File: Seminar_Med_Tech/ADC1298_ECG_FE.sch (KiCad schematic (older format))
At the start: 54 parts, among them J6 DB15_F-RA

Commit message: update anno
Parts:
- J4: renamed from J?; footprint (none) -> Pin_Headers:Pin_Header_Straight_1x02_Pitch2.54mm
- J8: renamed from J?; footprint (none) -> Pin_Headers:Pin_Header_Straight_1x10_Pitch2.54mm
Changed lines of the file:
@@
 AGND
 $Comp
-L CONN_01X10 J?
+L CONN_01X10 J8
 U 1 1 5947AEC5
 P 800 2100
-F 0 "J?" H 800 2650 50  0000 C CNN
+F 0 "J8" H 800 2650 50  0000 C CNN
 F 1 "CONN_01X10" V 900 2100 50  0000 C CNN
-F 2 "" H 800 2100 50  0001 C CNN
+F 2 "Pin_Headers:Pin_Header_Straight_1x10_Pitch2.54mm" H 800 2100 50  0001 C CNN
 F 3 "" H 800 2100 50  0001 C CNN
 	1    800  2100
@@
 Connection ~ 1750 5000
 $Comp
-L CONN_01X02 J?
+L CONN_01X02 J4
 U 1 1 59492CE6
 P 700 5050
-F 0 "J?" H 700 5200 50  0000 C CNN
+F 0 "J4" H 700 5200 50  0000 C CNN
 F 1 "CONN_01X02" V 800 5050 50  0000 C CNN
-F 2 "" H 700 5050 50  0001 C CNN
+F 2 "Pin_Headers:Pin_Header_Straight_1x02_Pitch2.54mm" H 700 5050 50  0001 C CNN
 F 3 "" H 700 5050 50  0001 C CNN
 	1    700  5050

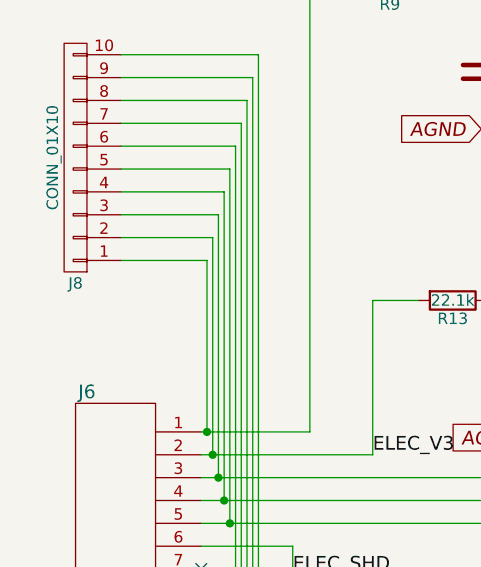
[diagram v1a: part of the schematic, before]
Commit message: Updated Schaltbild and changed BOM
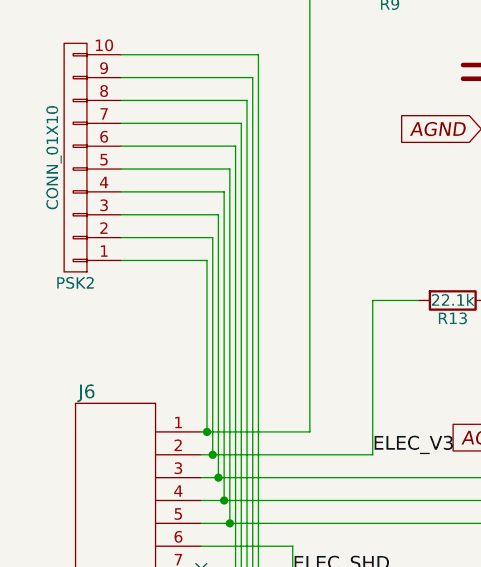
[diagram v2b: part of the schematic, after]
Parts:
- renumbered J8 to PSK2
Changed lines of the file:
@@
 AGND
 $Comp
-L CONN_01X10 J8
+L CONN_01X10 PSK2
 U 1 1 5947AEC5
 P 800 2100
-F 0 "J8" H 800 2650 50  0000 C CNN
+F 0 "PSK2" H 800 2650 50  0000 C CNN
 F 1 "CONN_01X10" V 900 2100 50  0000 C CNN
 F 2 "Pin_Headers:Pin_Header_Straight_1x10_Pitch2.54mm" H 800 2100 50  0001 C CNN

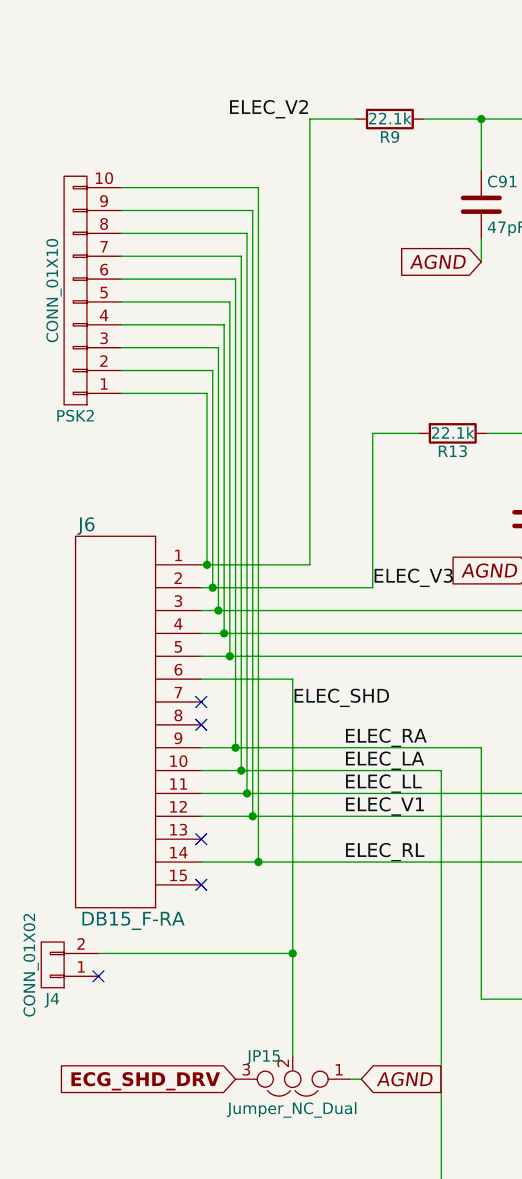
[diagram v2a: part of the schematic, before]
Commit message: Updated Schaltbild and added LM317 footprint
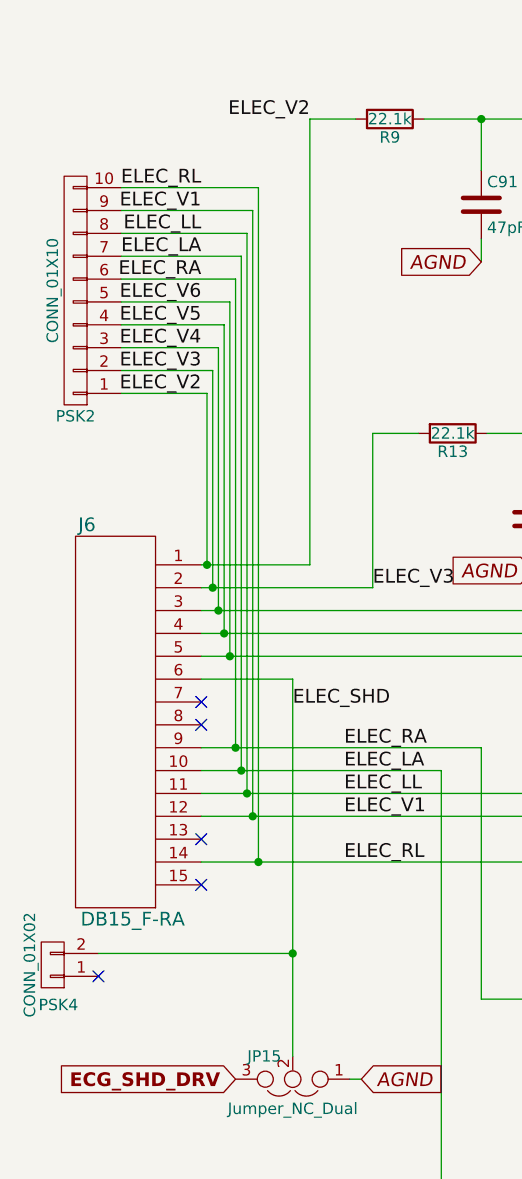
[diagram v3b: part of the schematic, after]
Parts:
- J6: footprint Pin_Headers:Pin_Header_Straight_1x15_Pitch2.54mm -> Connectors:DB15FC
- JP15: footprint jumper:jumper1x3 -> Jumper:jumper1x3
- PSK4: renamed from J4; footprint Pin_Headers:Pin_Header_Straight_1x02_Pitch2.54mm -> Pin_Headers:Pin_Header_Straight_1x03_Pitch2.54mm
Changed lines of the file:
@@
 F 0 "J6" H 850 6825 60  0000 C CNN
 F 1 "DB15_F-RA" H 1050 5100 60  0000 C CNN
-F 2 "Pin_Headers:Pin_Header_Straight_1x15_Pitch2.54mm" H 450 4975 60  0001 C CNN
+F 2 "Connectors:DB15FC" H 450 4975 60  0001 C CNN
 F 3 "" H 450 4975 60  0001 C CNN
 	1    450  4975
@@
 F 0 "JP15" H 1800 5450 50  0000 L CNN
 F 1 "Jumper_NC_Dual" H 1750 5650 50  0000 C BNN
-F 2 "jumper:jumper1x3" H 1750 5550 50  0001 C CNN
+F 2 "Jumper:jumper1x3" H 1750 5550 50  0001 C CNN
 F 3 "" H 1750 5550 50  0001 C CNN
 	1    1750 5550
@@
 Connection ~ 1750 5000
 $Comp
-L CONN_01X02 J4
+L CONN_01X02 PSK4
 U 1 1 59492CE6
 P 700 5050
-F 0 "J4" H 700 5200 50  0000 C CNN
+F 0 "PSK4" H 675 5225 50  0000 C CNN
 F 1 "CONN_01X02" V 800 5050 50  0000 C CNN
-F 2 "Pin_Headers:Pin_Header_Straight_1x02_Pitch2.54mm" H 700 5050 50  0001 C CNN
+F 2 "Pin_Headers:Pin_Header_Straight_1x03_Pitch2.54mm" H 700 5050 50  0001 C CNN
 F 3 "" H 700 5050 50  0001 C CNN
 	1    700  5050
@@
 $EndComp
 NoConn ~ 900  5100
+Text Label 1350 2550 2    60   ~ 0
+ELEC_V2
+Text Label 1350 2450 2    60   ~ 0
+ELEC_V3
+Text Label 1350 2350 2    60   ~ 0
+ELEC_V4
+Text Label 1350 2250 2    60   ~ 0
+ELEC_V5
+Text Label 1350 2150 2    60   ~ 0
+ELEC_V6
+Text Label 1350 2050 2    60   ~ 0
+ELEC_RA
+Text Label 1350 1850 2    60   ~ 0
+ELEC_LL
+Text Label 1350 1750 2    60   ~ 0
+ELEC_V1
+Text Label 1350 1650 2    60   ~ 0
+ELEC_RL
+Text Label 1350 1950 2    60   ~ 0
+ELEC_LA
 $EndSCHEMATC

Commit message: Update
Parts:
- D1, D10, D2, D3, D4, D5, D6, D7, D8, D9: footprint Diodes_SMD:D_SC-80_HandSoldering -> Diodes_SMD:D_SOD-123
- PSK4: footprint Pin_Headers:Pin_Header_Straight_1x03_Pitch2.54mm -> Pin_Headers:Pin_Header_Straight_1x02_Pitch2.54mm
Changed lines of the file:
@@
 F 0 "D1" H 3400 1075 50  0000 C CNN
 F 1 "D" H 3400 875 50  0000 C CNN
-F 2 "Diodes_SMD:D_SC-80_HandSoldering" H 3400 975 50  0001 C CNN
+F 2 "Diodes_SMD:D_SOD-123" H 3400 975 50  0001 C CNN
 F 3 "" H 3400 975 50  0001 C CNN
 	1    3400 975
@@
 F 0 "D5" H 6175 1100 50  0000 C CNN
 F 1 "D" H 6175 900 50  0000 C CNN
-F 2 "Diodes_SMD:D_SC-80_HandSoldering" H 6175 1000 50  0001 C CNN
+F 2 "Diodes_SMD:D_SOD-123" H 6175 1000 50  0001 C CNN
 F 3 "" H 6175 1000 50  0001 C CNN
 	1    6175 1000
@@
 F 0 "D10" H 9175 1050 50  0000 C CNN
 F 1 "D" H 9175 850 50  0000 C CNN
-F 2 "Diodes_SMD:D_SC-80_HandSoldering" H 9175 950 50  0001 C CNN
+F 2 "Diodes_SMD:D_SOD-123" H 9175 950 50  0001 C CNN
 F 3 "" H 9175 950 50  0001 C CNN
 	1    9175 950
@@
 F 0 "D2" H 3625 2500 50  0000 C CNN
 F 1 "D" H 3625 2300 50  0000 C CNN
-F 2 "Diodes_SMD:D_SC-80_HandSoldering" H 3625 2400 50  0001 C CNN
+F 2 "Diodes_SMD:D_SOD-123" H 3625 2400 50  0001 C CNN
 F 3 "" H 3625 2400 50  0001 C CNN
 	1    3625 2400
@@
 F 0 "D6" H 6200 2525 50  0000 C CNN
 F 1 "D" H 6200 2325 50  0000 C CNN
-F 2 "Diodes_SMD:D_SC-80_HandSoldering" H 6200 2425 50  0001 C CNN
+F 2 "Diodes_SMD:D_SOD-123" H 6200 2425 50  0001 C CNN
 F 3 "" H 6200 2425 50  0001 C CNN
 	1    6200 2425
@@
 F 0 "D9" H 9025 2500 50  0000 C CNN
 F 1 "D" H 9025 2300 50  0000 C CNN
-F 2 "Diodes_SMD:D_SC-80_HandSoldering" H 9025 2400 50  0001 C CNN
+F 2 "Diodes_SMD:D_SOD-123" H 9025 2400 50  0001 C CNN
 F 3 "" H 9025 2400 50  0001 C CNN
 	1    9025 2400
@@
 F 0 "D7" H 8325 4175 50  0000 C CNN
 F 1 "D" H 8325 3975 50  0000 C CNN
-F 2 "Diodes_SMD:D_SC-80_HandSoldering" H 8325 4075 50  0001 C CNN
+F 2 "Diodes_SMD:D_SOD-123" H 8325 4075 50  0001 C CNN
 F 3 "" H 8325 4075 50  0001 C CNN
 	1    8325 4075
@@
 F 0 "D8" H 9000 5225 50  0000 C CNN
 F 1 "D" H 9000 5025 50  0000 C CNN
-F 2 "Diodes_SMD:D_SC-80_HandSoldering" H 9000 5125 50  0001 C CNN
+F 2 "Diodes_SMD:D_SOD-123" H 9000 5125 50  0001 C CNN
 F 3 "" H 9000 5125 50  0001 C CNN
 	1    9000 5125
@@
 F 0 "D3" H 5125 5050 50  0000 C CNN
 F 1 "D" H 5125 4850 50  0000 C CNN
-F 2 "Diodes_SMD:D_SC-80_HandSoldering" H 5125 4950 50  0001 C CNN
+F 2 "Diodes_SMD:D_SOD-123" H 5125 4950 50  0001 C CNN
 F 3 "" H 5125 4950 50  0001 C CNN
 	1    5125 4950
@@
 F 0 "D4" H 5400 6075 50  0000 C CNN
 F 1 "D" H 5400 5875 50  0000 C CNN
-F 2 "Diodes_SMD:D_SC-80_HandSoldering" H 5400 5975 50  0001 C CNN
+F 2 "Diodes_SMD:D_SOD-123" H 5400 5975 50  0001 C CNN
 F 3 "" H 5400 5975 50  0001 C CNN
 	1    5400 5975
@@
 F 0 "PSK4" H 675 5225 50  0000 C CNN
 F 1 "CONN_01X02" V 800 5050 50  0000 C CNN
-F 2 "Pin_Headers:Pin_Header_Straight_1x03_Pitch2.54mm" H 700 5050 50  0001 C CNN
+F 2 "Pin_Headers:Pin_Header_Straight_1x02_Pitch2.54mm" H 700 5050 50  0001 C CNN
 F 3 "" H 700 5050 50  0001 C CNN
 	1    700  5050

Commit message: Update from develop
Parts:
- removed J6: DB15_F-RA, Connectors:DB15FC, symbol DB15_F-RA
- added J6: DB15_F-RA, symbol CONN_01X15
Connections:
- net ELEC_LA: now also J6.10 (P10)
- net ELEC_LL: now also J6.11 (P11)
- net ELEC_RA: now also J6.9 (P9)
- net ELEC_RL: now also J6.14 (P14)
- net ELEC_SHD: now also J6.6 (P6)
- net ELEC_V1: now also J6.12 (P12)
- net ELEC_V2: now also J6.1 (P1)
- net ELEC_V3: now also J6.2 (P2)
- net ELEC_V4: now also J6.3 (P3)
- net ELEC_V5: now also J6.4 (P4)
- net ELEC_V6: now also J6.5 (P5)
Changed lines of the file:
@@
 $EndDescr
-$Comp
-L DB15_F-RA J6
-U 1 1 59454B8D
-P 450 4975
-F 0 "J6" H 850 6825 60  0000 C CNN
-F 1 "DB15_F-RA" H 1050 5100 60  0000 C CNN
-F 2 "Connectors:DB15FC" H 450 4975 60  0001 C CNN
-F 3 "" H 450 4975 60  0001 C CNN
-	1    450  4975
-	1    0    0    -1
-$EndComp
 $Comp
 L R R9
@@
 Text Label 1350 1950 2    60   ~ 0
 ELEC_LA
+$Comp
+L CONN_01X15 J6
+U 1 1 594BFFB9
+P 1150 4000
+F 0 "J6" H 1150 4800 50  0000 C CNN
+F 1 "DB15_F-RA" V 1250 4000 50  0000 C CNN
+F 2 "" H 1150 4000 50  0001 C CNN
+F 3 "" H 1150 4000 50  0001 C CNN
+	1    1150 4000
+	-1   0    0    -1
+$EndComp
 $EndSCHEMATC

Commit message: Update
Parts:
- J6: footprint (none) -> Connectors:DB15FC
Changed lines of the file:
@@
 F 0 "J6" H 1150 4800 50  0000 C CNN
 F 1 "DB15_F-RA" V 1250 4000 50  0000 C CNN
-F 2 "" H 1150 4000 50  0001 C CNN
+F 2 "Connectors:DB15FC" H 1150 4000 50  0001 C CNN
 F 3 "" H 1150 4000 50  0001 C CNN
 	1    1150 4000

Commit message: Update
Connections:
- net ELEC_LA: now also PSK2.9 (P9); no longer PSK2.7 (P7)
- net ELEC_RA: now also PSK2.10 (P10); no longer PSK2.6 (P6)
- net ELEC_RL: now also PSK2.6 (P6); no longer PSK2.10 (P10)
- net ELEC_V1: now also PSK2.7 (P7); no longer PSK2.9 (P9)
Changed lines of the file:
@@
 Wire Wire Line
 	1000 2050 1500 2050
-Wire Wire Line
-	1500 2050 1500 4100
-Connection ~ 1500 4100
+Connection ~ 1500 4600
 Wire Wire Line
 	1000 1950 1525 1950
 Wire Wire Line
-	1525 1950 1525 4200
-Connection ~ 1525 4200
-Wire Wire Line
 	1000 1850 1550 1850
 Wire Wire Line
-	1550 1850 1550 4300
+	1000 1750 1575 1750
 Connection ~ 1550 4300
 Wire Wire Line
-	1000 1750 1575 1750
-Wire Wire Line
-	1575 1750 1575 4400
-Connection ~ 1575 4400
-Wire Wire Line
 	1000 1650 1600 1650
-Wire Wire Line
-	1600 1650 1600 4600
-Connection ~ 1600 4600
+Connection ~ 1575 4200
 Wire Wire Line
 	900  5000 1750 5000
@@
 ELEC_V6
 Text Label 1350 2050 2    60   ~ 0
-ELEC_RA
+ELEC_RL
 Text Label 1350 1850 2    60   ~ 0
 ELEC_LL
-Text Label 1350 1750 2    60   ~ 0
+Text Label 1350 1950 2    60   ~ 0
 ELEC_V1
 Text Label 1350 1650 2    60   ~ 0
-ELEC_RL
-Text Label 1350 1950 2    60   ~ 0
+ELEC_RA
+Text Label 1350 1750 2    60   ~ 0
 ELEC_LA
 $Comp
@@
 	-1   0    0    -1
 $EndComp
+Wire Wire Line
+	1500 2050 1500 4600
+Wire Wire Line
+	1525 1950 1525 4400
+Connection ~ 1525 4400
+Wire Wire Line
+	1550 1850 1550 4300
+Wire Wire Line
+	1550 4300 1625 4300
+Wire Wire Line
+	1575 1750 1575 4200
+Wire Wire Line
+	1575 4200 1625 4200
+Wire Wire Line
+	1600 1650 1600 4100
+Connection ~ 1600 4100
 $EndSCHEMATC

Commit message: Update
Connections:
- net ELEC_RA: now also PSK2.7 (P7); no longer PSK2.10 (P10)
- net ELEC_RL: now also PSK2.1 (P1); no longer PSK2.6 (P6)
- net ELEC_V1: now also PSK2.2 (P2); no longer PSK2.7 (P7)
- net ELEC_V2: now also PSK2.6 (P6); no longer PSK2.1 (P1)
- net ELEC_V3: now also PSK2.5 (P5); no longer PSK2.2 (P2)
- net ELEC_V4: now also PSK2.4 (P4); no longer PSK2.3 (P3)
- net ELEC_V5: now also PSK2.3 (P3); no longer PSK2.4 (P4)
- net ELEC_V6: now also PSK2.10 (P10); no longer PSK2.5 (P5)
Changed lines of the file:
@@
 	1350 4600 6275 4600
 Wire Wire Line
-	1350 4200 2400 4200
-Wire Wire Line
 	2400 4200 2400 6150
 Wire Wire Line
@@
 	1350 4100 2575 4100
 Wire Wire Line
-	1350 4300 6625 4300
-Wire Wire Line
 	7175 2650 7650 2650
 Wire Wire Line
@@
 Wire Wire Line
 	4575 3600 4575 2675
-Wire Wire Line
-	1350 3600 4575 3600
 Wire Wire Line
 	1350 3700 6825 3700
@@
 Wire Wire Line
 	2100 3400 2100 2725
-Wire Wire Line
-	1350 3400 2100 3400
 Connection ~ 3625 2725
 Wire Wire Line
@@
 	2000 5550 2050 5550
 Wire Wire Line
-	1375 3300 1375 2550
-Wire Wire Line
 	1375 2550 1000 2550
-Connection ~ 1375 3300
 Wire Wire Line
 	1000 2450 1400 2450
 Wire Wire Line
-	1400 2450 1400 3400
-Connection ~ 1400 3400
-Wire Wire Line
-	1000 2350 1425 2350
-Wire Wire Line
-	1425 2350 1425 3500
-Connection ~ 1425 3500
-Wire Wire Line
 	1000 2250 1450 2250
 Wire Wire Line
-	1450 2250 1450 3600
-Connection ~ 1450 3600
-Wire Wire Line
 	1000 2150 1475 2150
 Wire Wire Line
-	1475 2150 1475 3700
-Connection ~ 1475 3700
-Wire Wire Line
 	1000 2050 1500 2050
-Connection ~ 1500 4600
 Wire Wire Line
 	1000 1950 1525 1950
@@
 $EndComp
 NoConn ~ 900  5100
-Text Label 1350 2550 2    60   ~ 0
+Text Label 50   3675 2    60   ~ 0
 ELEC_V2
-Text Label 1350 2450 2    60   ~ 0
+Text Label -600 3575 2    60   ~ 0
 ELEC_V3
-Text Label 1350 2350 2    60   ~ 0
+Text Label -850 3125 2    60   ~ 0
 ELEC_V4
-Text Label 1350 2250 2    60   ~ 0
+Text Label -1050 2650 2    60   ~ 0
 ELEC_V5
-Text Label 1350 2150 2    60   ~ 0
+Text Label -175 3250 2    60   ~ 0
 ELEC_V6
-Text Label 1350 2050 2    60   ~ 0
+Text Label 25   2900 2    60   ~ 0
 ELEC_RL
-Text Label 1350 1850 2    60   ~ 0
+Text Label 25   2250 2    60   ~ 0
 ELEC_LL
-Text Label 1350 1950 2    60   ~ 0
+Text Label -200 2625 2    60   ~ 0
 ELEC_V1
-Text Label 1350 1650 2    60   ~ 0
+Text Label -75  1775 2    60   ~ 0
 ELEC_RA
-Text Label 1350 1750 2    60   ~ 0
+Text Label 125  2125 2    60   ~ 0
 ELEC_LA
 $Comp
@@
 $EndComp
 Wire Wire Line
-	1500 2050 1500 4600
-Wire Wire Line
-	1525 1950 1525 4400
-Connection ~ 1525 4400
+	1525 1950 1525 4100
 Wire Wire Line
 	1550 1850 1550 4300
 Wire Wire Line
-	1550 4300 1625 4300
-Wire Wire Line
 	1575 1750 1575 4200
 Wire Wire Line
-	1575 4200 1625 4200
-Wire Wire Line
-	1600 1650 1600 4100
-Connection ~ 1600 4100
+	1350 4200 2400 4200
+Wire Wire Line
+	1375 2550 1375 4600
+Connection ~ 1375 4600
+Wire Wire Line
+	1350 3400 2100 3400
+Wire Wire Line
+	1400 2450 1400 4400
+Connection ~ 1400 4400
+Wire Wire Line
+	1450 2250 1450 3500
+Wire Wire Line
+	1350 3600 4575 3600
+Wire Wire Line
+	1000 2350 1425 2350
+Wire Wire Line
+	1425 2350 1425 3600
+Connection ~ 1425 3600
+Connection ~ 1450 3500
+Wire Wire Line
+	1475 2150 1475 3400
+Connection ~ 1475 3400
+Wire Wire Line
+	1500 2050 1500 3300
+Connection ~ 1500 3300
+Connection ~ 1525 4100
+Wire Wire Line
+	1600 1650 1600 3700
+Connection ~ 1600 3700
+Wire Wire Line
+	1350 4300 6625 4300
 $EndSCHEMATC
